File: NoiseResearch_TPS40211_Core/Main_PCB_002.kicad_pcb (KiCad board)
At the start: 2 copper layers, 133.3 x 96.5 mm, 42 parts, among them IC1 TPS40211QDGQRQ1, Q1 AON7407, U12 MCP9700AT-ETT, U13 MCP9700AT-ETT, U2 Mounting_Hole_M2, U3 Mounting_Hole_M2, U4 Mounting_Hole_M2, U5 Mounting_Hole_M2

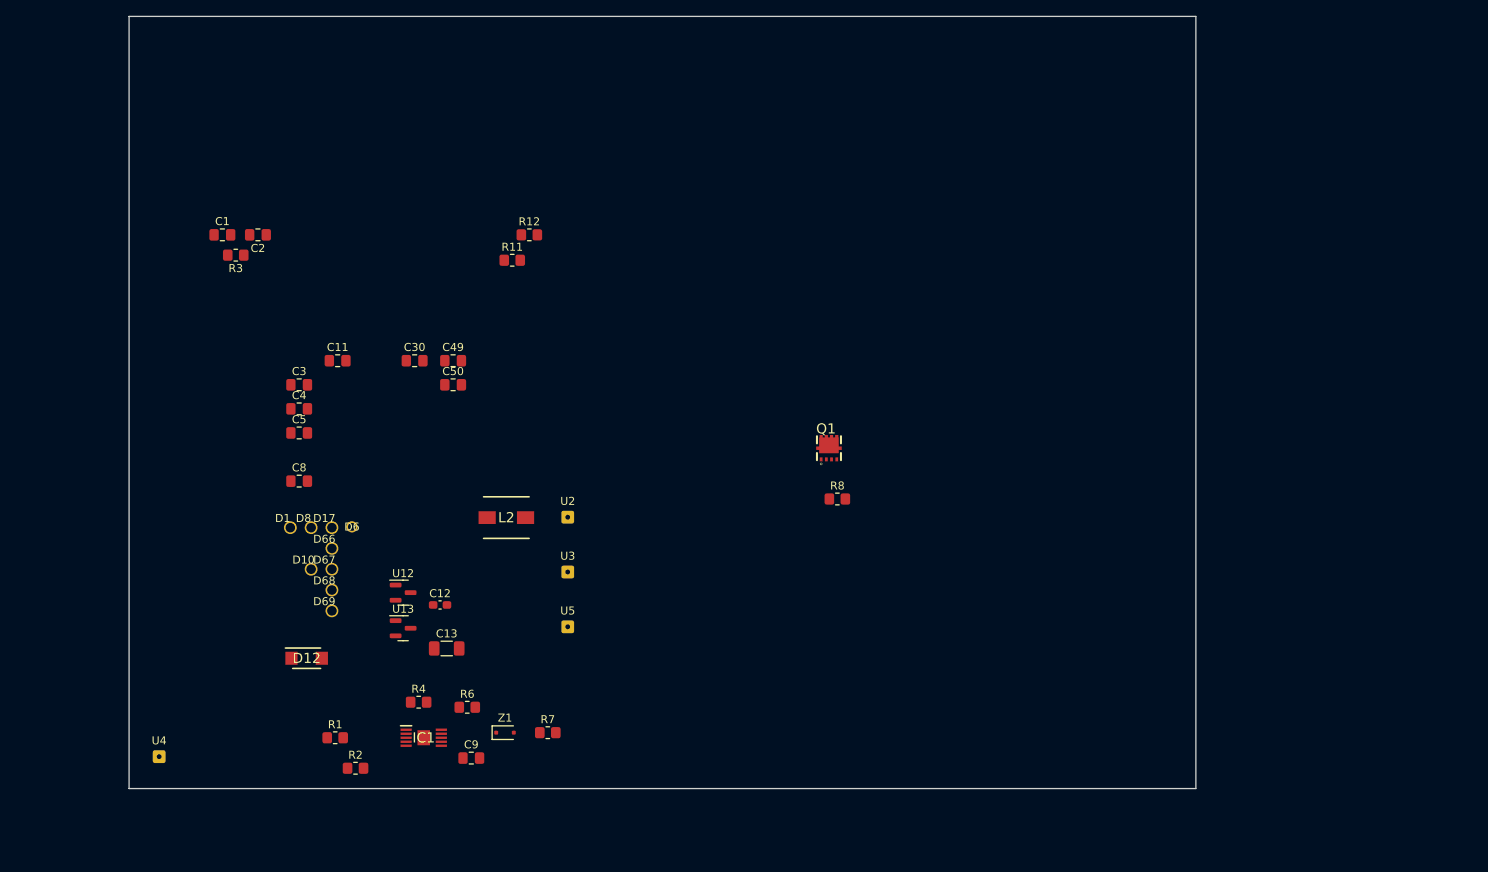
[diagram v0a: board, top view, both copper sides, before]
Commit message: Noise research for TSP40211 004
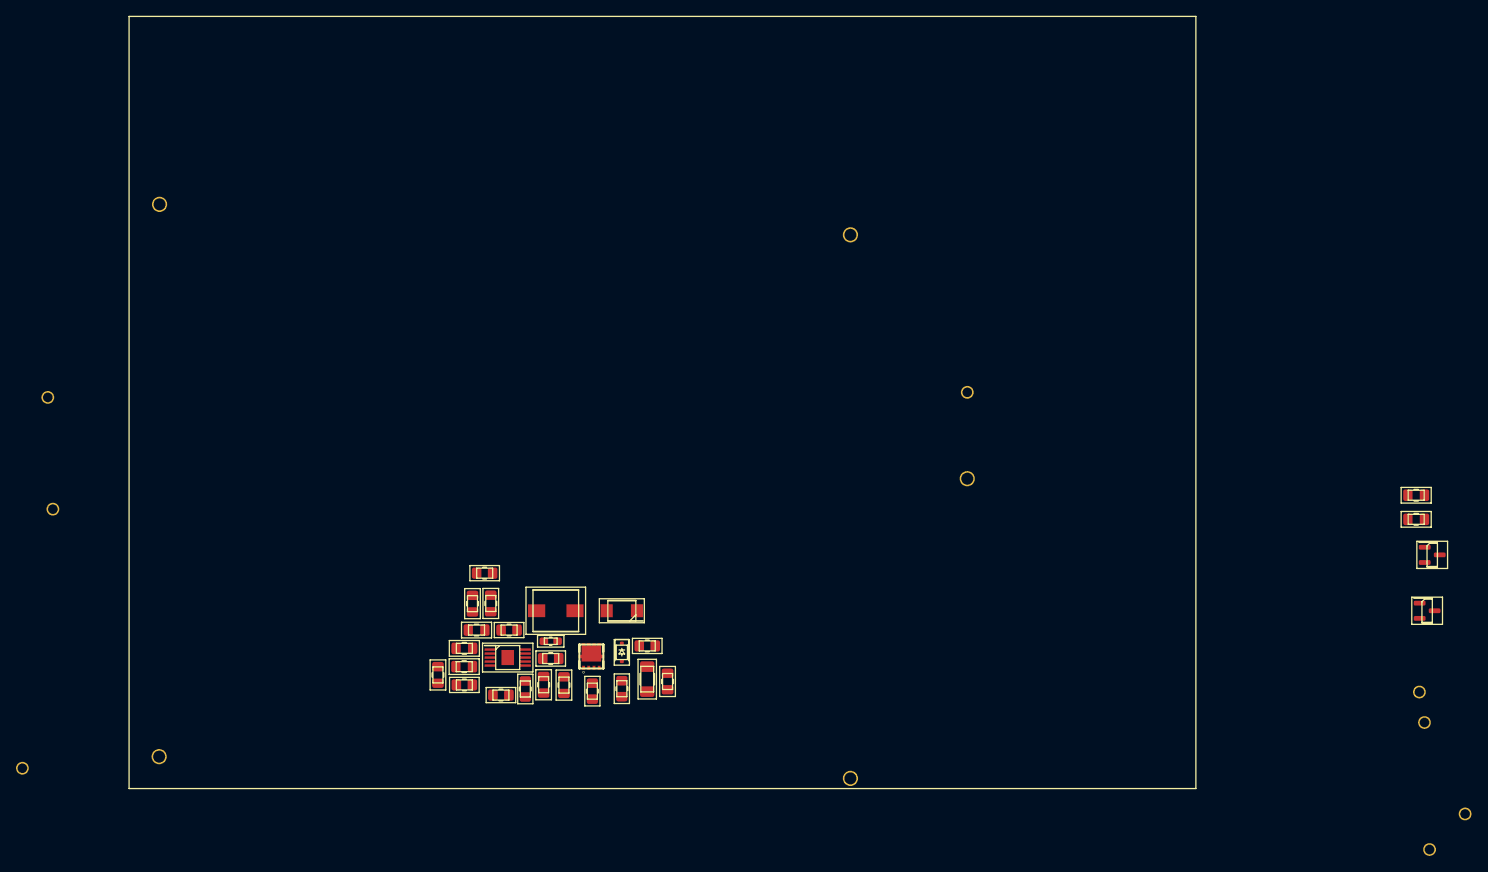
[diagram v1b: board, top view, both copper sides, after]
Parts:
- D6: footprint Flat_Wires_Pads:Wire_Hole_1mm -> Wire_holes:WireHole_1p5
- U2, U3, U4, U5: footprint Connector_Wire:SolderWire-0.1sqmm_1x01_D0.4mm_OD1mm -> Wire_holes:WireHole_1p5
- moved D68 144.4 mm to (230.5, 153.0)
- moved D69 140.4 mm to (226.1, 157.5)
- moved D67 137.9 mm to (225.4, 141.6)
- moved D66 137.1 mm to (224.8, 137.8)
- moved U12 128.7 mm to (226.4, 120.7)
- moved U13 128.0 mm to (225.8, 127.6)
- moved C49 121.6 mm to (224.4, 113.2)
- moved C50 121.6 mm to (224.4, 116.2)
- moved D10 84.9 mm to (168.3, 100.3)
- moved D6 77.2 mm to (168.3, 111.1)
- moved U5 73.4 mm to (67.3, 76.8)
- moved C1 61.3 mm to (102.1, 135.7), turned to 90 degrees
- moved R3 60.8 mm to (105.4, 136.9)
- moved C2 59.8 mm to (105.4, 134.6)
- moved R12 53.5 mm to (128.3, 132.0), turned to 180 degrees
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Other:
- board outline removed

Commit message: Noise research for TSP40211 004
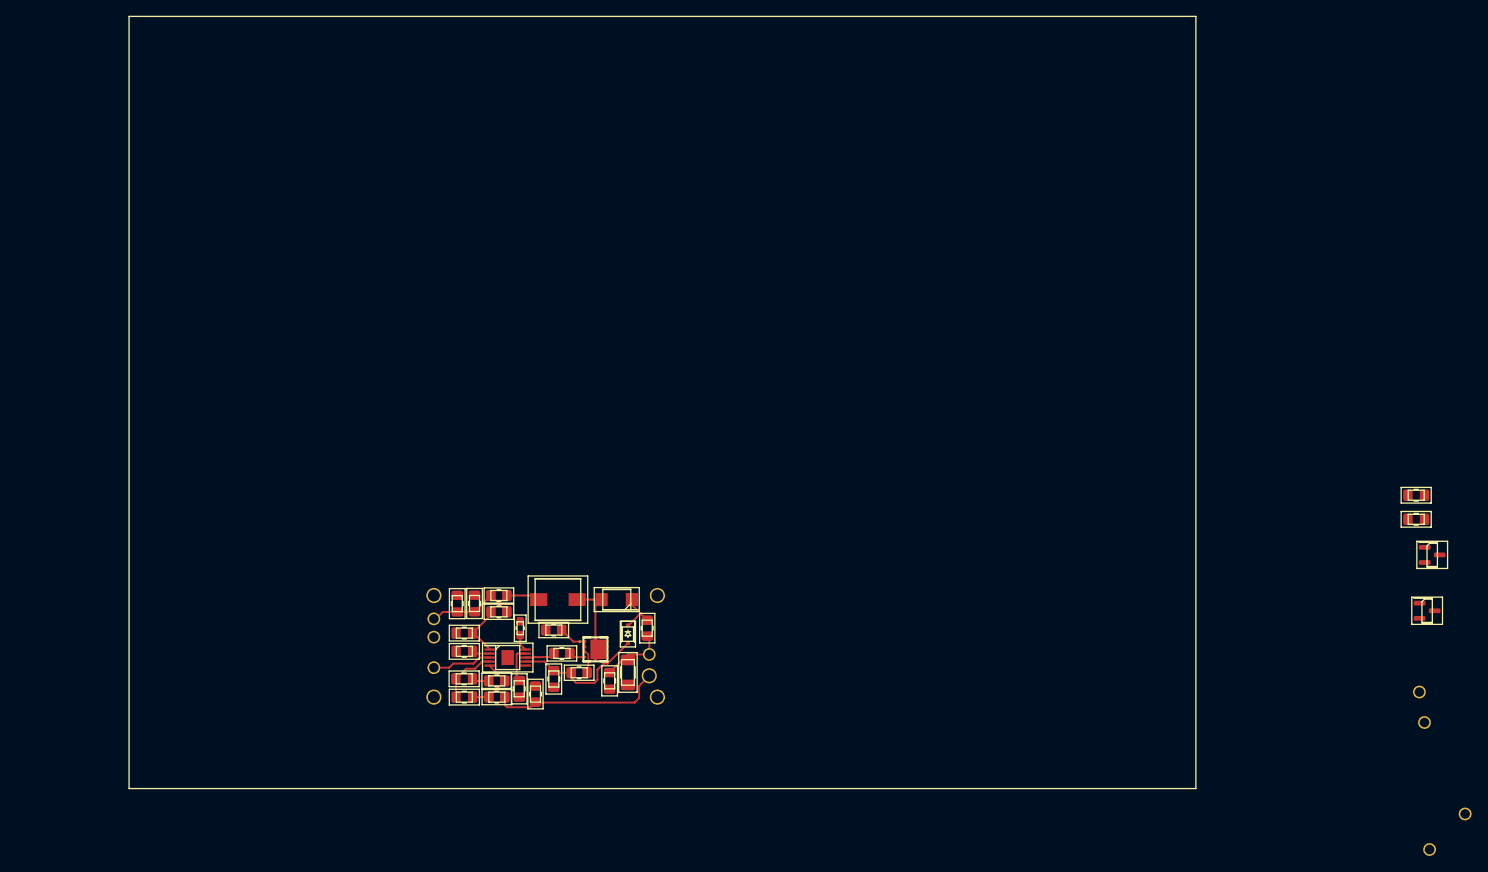
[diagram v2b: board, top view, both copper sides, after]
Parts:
- moved U5 59.7 mm to (101.6, 125.7)
- moved D8 55.6 mm to (101.6, 128.7)
- moved D17 52.9 mm to (101.6, 134.7)
- moved D10 51.5 mm to (128.5, 133.1)
- moved U2 51.1 mm to (129.5, 125.7)
- moved D1 50.2 mm to (101.6, 130.9)
- moved D6 46.8 mm to (128.5, 135.8)
- moved U4 35.1 mm to (101.6, 138.4)
- moved U3 26.2 mm to (129.5, 138.4)
- moved R8 9.03 mm to (116.6, 130.0), turned to 180 degrees
- moved C30 7.24 mm to (123.6, 136.4)
- moved R7 5.70 mm to (119.8, 135.4), turned to 0 degrees
- moved C9 5.61 mm to (112.3, 137.4)
- moved C1 4.31 mm to (105.4, 138.4), turned to 180 degrees
- moved C12 4.14 mm to (112.4, 129.8), turned to 90 degrees
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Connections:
- C11 pad 2: Net-(D1-Conn) -> GND
- C12 pad 2: Net-(D1-Conn) -> GND
- C13 pad 2: Net-(D1-Conn) -> GND
- C3 pad 1: Net-(D1-Conn) -> GND
- C30 pad 2: Net-(D1-Conn) -> GND
- C4 pad 1: Net-(D1-Conn) -> GND
- C49 pad 2: Net-(D1-Conn) -> GND
- C5 pad 2: Net-(D1-Conn) -> GND
- C50 pad 2: Net-(D1-Conn) -> GND
- C8 pad 2: Net-(D1-Conn) -> GND
- C9 pad 2: Net-(D1-Conn) -> GND
- D1 pad 1: Net-(D1-Conn) -> GND
- D69 pad 1: Net-(D1-Conn) -> GND
- IC1 pad 11: Net-(D1-Conn) -> GND
- IC1 pad 6: Net-(D1-Conn) -> GND
- Q1 pad 10: (no net) -> Net-(Q1-D_1)
- Q1 pad 11: (no net) -> Net-(Q1-D_1)
- Q1 pad 9: (no net) -> Net-(Q1-D_1)
- R1 pad 1: Net-(D1-Conn) -> GND
- R8 pad 2: Net-(D1-Conn) -> GND
- U12 pad 3: Net-(D1-Conn) -> GND
- U13 pad 3: Net-(D1-Conn) -> GND
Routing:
- net Net-(D6-Conn): track 0.00 -> 22.3 mm
- net Net-(IC1-ISNS): track 0.00 -> 17.2 mm
- net Net-(D8-Conn): track 0.00 -> 13.3 mm
- net Net-(Q1-D_1): track 0.00 -> 9.28 mm
- net Net-(D10-Conn): track 0.00 -> 8.54 mm
- net Net-(Q1-S_1): track 0.00 -> 7.69 mm
- net Net-(D17-Conn): track 0.00 -> 7.55 mm
- net Net-(IC1-FB): track 0.00 -> 7.55 mm
- net Net-(IC1-COMP): track 0.00 -> 7.47 mm
- net Net-(IC1-RC): track 0.00 -> 6.65 mm
- net Net-(Z1-K): track 0.00 -> 5.77 mm
- net Net-(IC1-BP): track 0.00 -> 4.65 mm
- net Net-(L2-Pad1): track 0.00 -> 4.19 mm
- net Net-(IC1-GDRV): track 0.00 -> 4.10 mm
- net Net-(IC1-SS): track 0.00 -> 2.29 mm
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
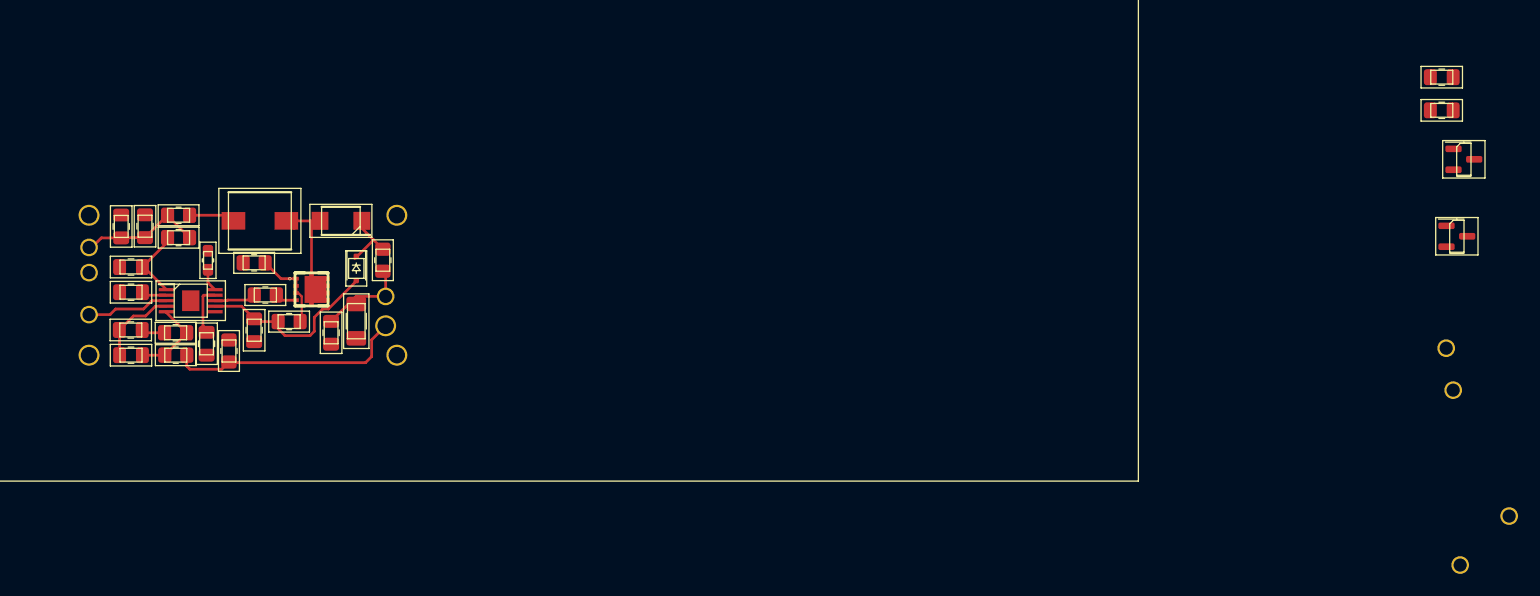
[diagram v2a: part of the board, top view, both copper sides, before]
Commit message: Noise research for TSP40211 005
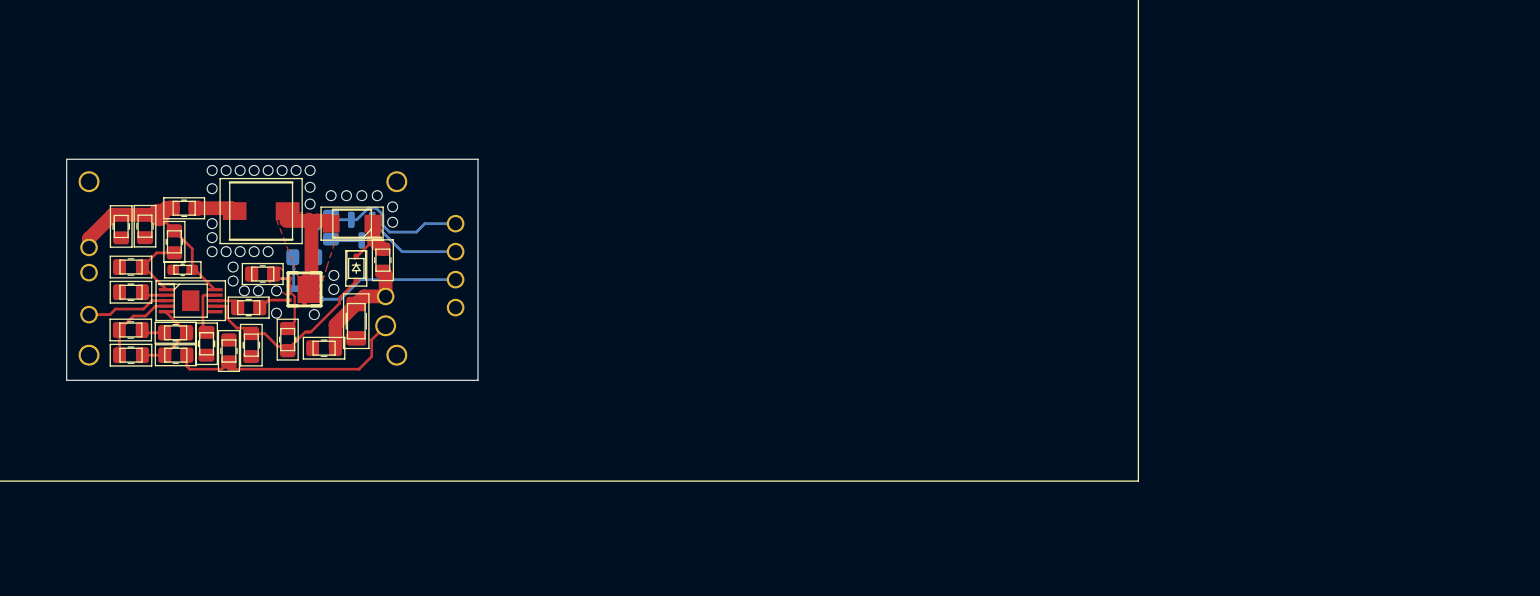
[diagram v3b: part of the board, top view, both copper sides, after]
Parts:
- C49, C50, U12, U13: moved to B.Cu
- moved U13 104.6 mm to (121.2, 132.4), turned to 180 degrees
- moved C49 104.5 mm to (121.1, 129.5), turned to 180 degrees
- moved C50 101.4 mm to (123.6, 126.9), turned to -90 degrees
- moved U12 100.2 mm to (126.4, 127.1), turned to -90 degrees
- moved D68 98.6 mm to (134.9, 129.0)
- moved D69 94.1 mm to (134.9, 134.1)
- moved D67 91.1 mm to (134.9, 131.6)
- moved D66 90.6 mm to (134.9, 126.5)
- moved U2 3.05 mm to (129.5, 122.7)
- moved U5 3.05 mm to (101.6, 122.7)
- moved C12 2.44 mm to (110.1, 130.7), turned to 180 degrees
- moved R6 1.89 mm to (116.1, 134.1)
- moved R7 1.64 mm to (119.6, 137.0), turned to 90 degrees
- moved C30 1.53 mm to (122.9, 137.8), turned to 180 degrees
- moved C11 1.38 mm to (116.3, 137.5)
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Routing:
- net Net-(D66-Conn): track 0.00 -> 19.6 mm
- net Net-(D67-Conn): track 0.00 -> 13.4 mm, vias 0 -> 1
- net Net-(D68-Conn): track 0.00 -> 8.87 mm
- net GND: track 0.02 -> 5.77 mm
- net Net-(D8-Conn): track 13.3 -> 18.6 mm
- net Net-(IC1-GDRV): track 4.10 -> 2.04 mm
- net Net-(D10-Conn): track 8.54 -> 10.1 mm
- net Net-(Q1-S_1): track 7.69 -> 6.52 mm
- net Net-(Q1-G): track 1.98 -> 2.83 mm
- net (no net): vias 0 -> 32
- added copper zone on F.Cu, net Net-(Q1-D_1)
- added copper zone on F.Cu, net Net-(Q1-S_1)
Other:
- board outline added: 37.3 x 20.1 mm
